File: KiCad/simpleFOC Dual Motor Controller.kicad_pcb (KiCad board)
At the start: 4 copper layers, 50 x 50 mm, 126 parts, among them CN101 XT60PB-F.G.Y, CN201 MR60-F, CN202 MR60-F, J101 Conn_01x04, J103 Conn_01x06, J104 Conn_01x06, J105 USB-TYPE-C-019, Q101 AO3400A, Q301 XRS100N06LD, Q302 XRS100N06LD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

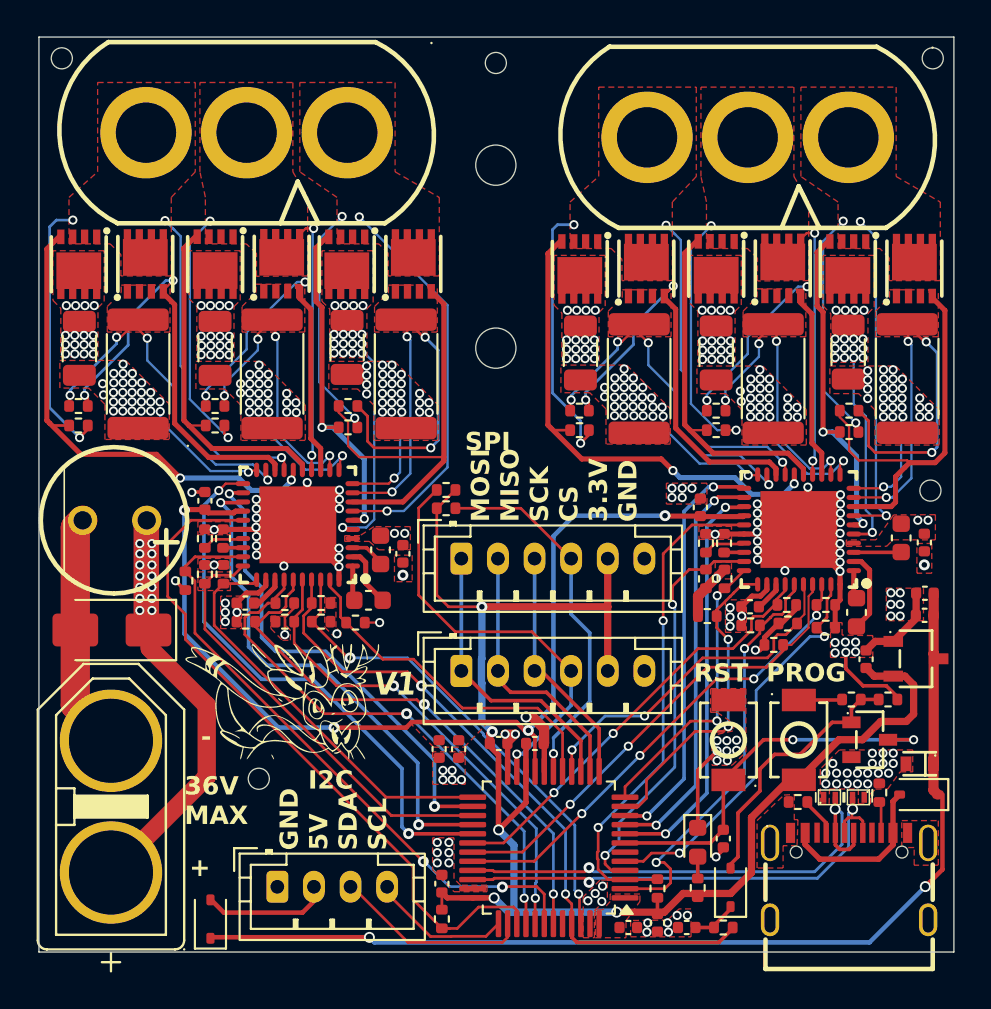
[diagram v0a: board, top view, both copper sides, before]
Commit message: added bulk ceramic capacitance
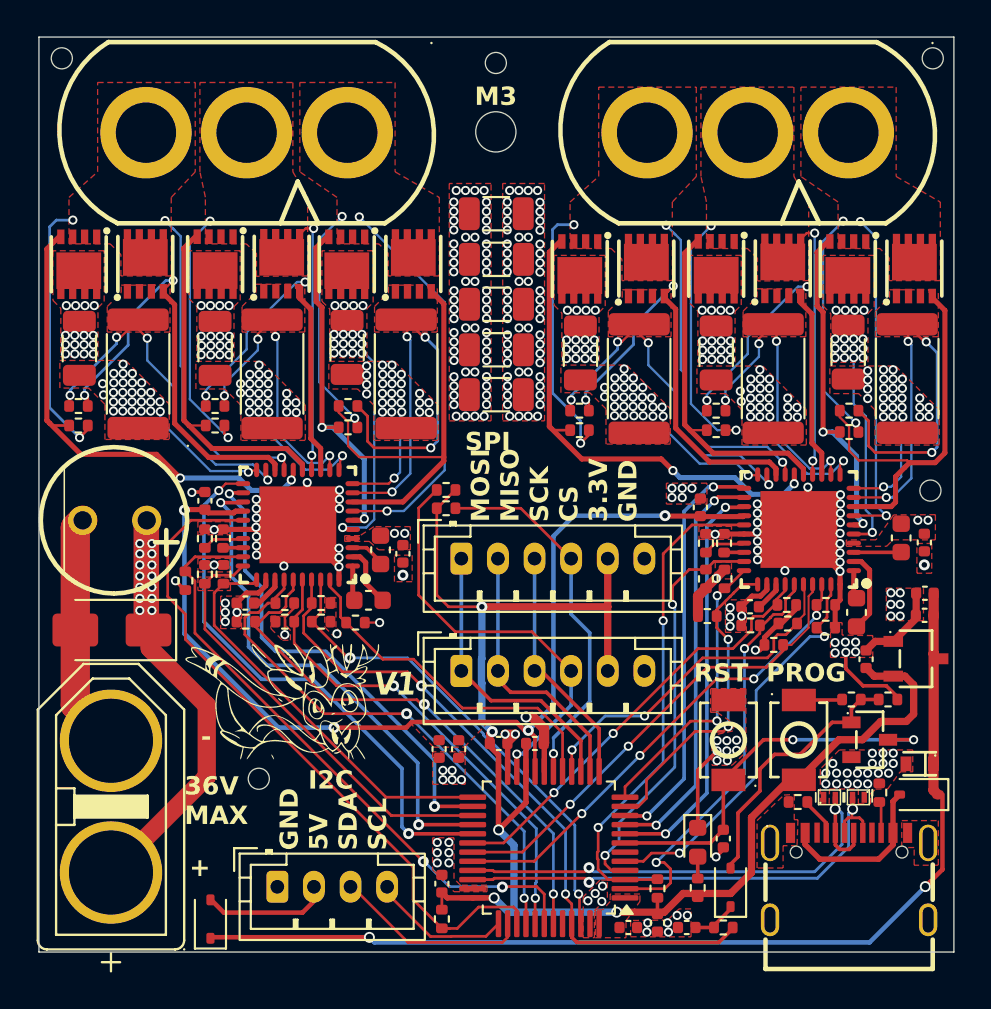
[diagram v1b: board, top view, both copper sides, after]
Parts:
- removed H106: MountingHole, MountingHole:MountingHole_2.2mm_M2
- added C117: 10u, Capacitor_SMD:C_1206_3216Metric, F.Cu at (125.0, 34.7)
- added C118: 10u, Capacitor_SMD:C_1206_3216Metric, F.Cu at (125.0, 37.1)
- added C119: 10u, Capacitor_SMD:C_1206_3216Metric, F.Cu at (125.0, 39.6)
- added C120: 10u, Capacitor_SMD:C_1206_3216Metric, F.Cu at (125.0, 42.1)
- added C121: 10u, Capacitor_SMD:C_1206_3216Metric, F.Cu at (125.0, 44.5)
- moved H105 1.82 mm to (125.0, 30.2)
- moved CN201 0.25 mm to (138.7, 30.2)
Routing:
- net M+: vias 116 -> 172
- net GND: vias 274 -> 330
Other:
- board text added: "M3"
